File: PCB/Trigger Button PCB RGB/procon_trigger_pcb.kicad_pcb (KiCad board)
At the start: 2 copper layers, 110.3 x 46.3 mm, 10 parts, among them J1 Conn_01x05_Pin, J2 Conn_01x05_Pin, SW1 SW_Push, SW2 SW_Push, SW3 SW_Push, SW4 SW_Push

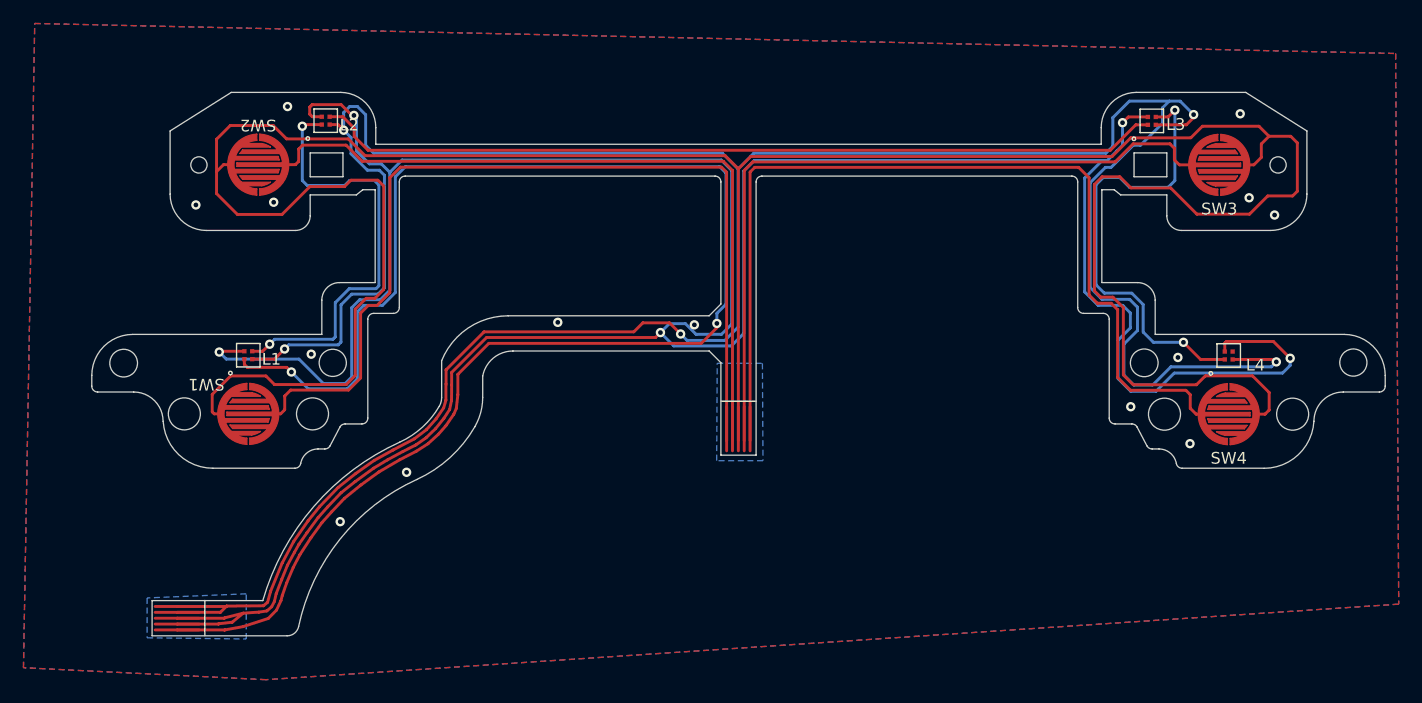
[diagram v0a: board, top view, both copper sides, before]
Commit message: Added switch to trigger board
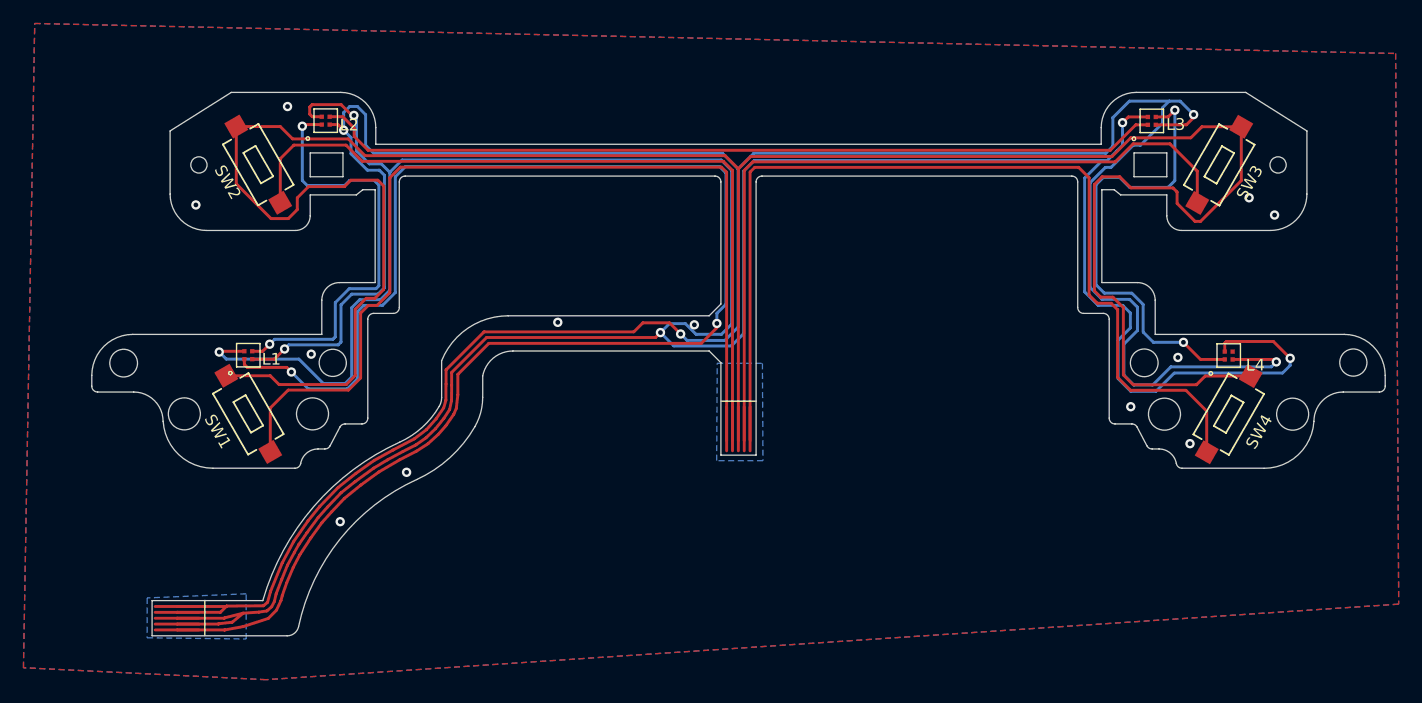
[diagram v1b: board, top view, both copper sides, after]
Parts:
- SW1, SW2, SW3, SW4: footprint hhl:starprint -> hhl:SW-SMD_L6.0-W3.5-LS8.0_TS04-TBW1FH4.3
- turned SW1 to 120 degrees
- turned SW2 to 120 degrees
- turned SW3 to 60 degrees
- turned SW4 to 60 degrees
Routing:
- net Scan_D: track 237.1 -> 212.2 mm
- net R_Pull: track 63.4 -> 66.7 mm
- net ZR_Pull: track 80.0 -> 83.2 mm
- net ZL_Pull: track 80.2 -> 83.3 mm
- net L_Pull: track 63.5 -> 66.3 mm
- net GND: vias 19 -> 17
